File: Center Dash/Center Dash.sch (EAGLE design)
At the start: 55 parts, among them J1 502585-0470, U2 TPS54540DDARQ1

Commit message: Fixed Ashers fuck up
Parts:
- added R3, R5, R9: 100, rcl:R-US_R0805
- C1, C11, C13, C14, C15, C16, C2, C3, C4, C5, C6, C7: value (none) -> 10uF; device rcl:C-USC0402 -> rcl:C-USC0603K; PARTNO (none) -> GRM188R61A106KE69D
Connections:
- removed net SPARE_4: U$1.P7, U$2.36/A17
- removed net SPARE_5: U$1.P6, U$2.37/A18
- new net IGNITION_1: R5.2, U$1.P12, U$2.33/A14
- new net IGNITION_2: R3.2, U$1.P11, U$2.34/A15
- new net N$11: LED1.DI, R9.1
- net +3V3: now also R3.1, R5.1
- net DI1: now also R9.2; no longer LED1.DI
- net SPARE_1: now also U$1.P8, U$2.35/A16; no longer U$1.P12, U$2.33/A14
- net SPARE_2: now also U$1.P7, U$2.36/A17; no longer U$1.P11, U$2.34/A15
- net SPARE_3: now also U$1.P6, U$2.37/A18; no longer U$1.P8, U$2.35/A16
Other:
- moved on the sheet: C1, C11, C13, C14, C15, C16, C2, C3, C4, C5, C6, C7

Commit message: Made changes
Change LED caps to .1uF on right ear and center
Add resistor to D2
Add level shifters (1 for D1, 1 for D2)
Add mount holes on right ear
Add mosfet for servo (see things to consider.txt)
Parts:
- added R11: 100, rcl:R-US_R0805
- C1, C11, C13, C14, C15, C16, C2, C3, C4, C5, C6, C7: value 10uF -> .1uF
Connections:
- new net DI2_MORE: R11.1, U$1.P4
- net DI2: now also R11.2; no longer U$1.P4
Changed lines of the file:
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@@
 <?xml version="1.0" encoding="utf-8"?>
 <!DOCTYPE eagle SYSTEM "eagle.dtd">
-<eagle version="8.5.0">
+<eagle version="8.3.1">
 <drawing>
 <settings>
@@
 <part name="+3V1" library="supply1" library_urn="urn:adsk.eagle:library:371" deviceset="+3V3" device=""/>
 <part name="R9" library="rcl" deviceset="R-US_" device="R0805" value="100"/>
-<part name="C1" library="rcl" deviceset="C-US" device="C0603K" value="10uF">
+<part name="C1" library="rcl" deviceset="C-US" device="C0603K" value=".1uF">
 <attribute name="PARTNO" value="GRM188R61A106KE69D"/>
 </part>
-<part name="C2" library="rcl" deviceset="C-US" device="C0603K" value="10uF">
+<part name="C2" library="rcl" deviceset="C-US" device="C0603K" value=".1uF">
 <attribute name="PARTNO" value="GRM188R61A106KE69D"/>
 </part>
-<part name="C3" library="rcl" deviceset="C-US" device="C0603K" value="10uF">
+<part name="C3" library="rcl" deviceset="C-US" device="C0603K" value=".1uF">
 <attribute name="PARTNO" value="GRM188R61A106KE69D"/>
 </part>
-<part name="C4" library="rcl" deviceset="C-US" device="C0603K" value="10uF">
+<part name="C4" library="rcl" deviceset="C-US" device="C0603K" value=".1uF">
 <attribute name="PARTNO" value="GRM188R61A106KE69D"/>
 </part>
-<part name="C5" library="rcl" deviceset="C-US" device="C0603K" value="10uF">
+<part name="C5" library="rcl" deviceset="C-US" device="C0603K" value=".1uF">
 <attribute name="PARTNO" value="GRM188R61A106KE69D"/>
 </part>
-<part name="C6" library="rcl" deviceset="C-US" device="C0603K" value="10uF">
+<part name="C6" library="rcl" deviceset="C-US" device="C0603K" value=".1uF">
 <attribute name="PARTNO" value="GRM188R61A106KE69D"/>
 </part>
-<part name="C7" library="rcl" deviceset="C-US" device="C0603K" value="10uF">
+<part name="C7" library="rcl" deviceset="C-US" device="C0603K" value=".1uF">
 <attribute name="PARTNO" value="GRM188R61A106KE69D"/>
 </part>
-<part name="C11" library="rcl" deviceset="C-US" device="C0603K" value="10uF">
+<part name="C11" library="rcl" deviceset="C-US" device="C0603K" value=".1uF">
 <attribute name="PARTNO" value="GRM188R61A106KE69D"/>
 </part>
-<part name="C13" library="rcl" deviceset="C-US" device="C0603K" value="10uF">
+<part name="C13" library="rcl" deviceset="C-US" device="C0603K" value=".1uF">
 <attribute name="PARTNO" value="GRM188R61A106KE69D"/>
 </part>
-<part name="C14" library="rcl" deviceset="C-US" device="C0603K" value="10uF">
+<part name="C14" library="rcl" deviceset="C-US" device="C0603K" value=".1uF">
 <attribute name="PARTNO" value="GRM188R61A106KE69D"/>
 </part>
-<part name="C15" library="rcl" deviceset="C-US" device="C0603K" value="10uF">
+<part name="C15" library="rcl" deviceset="C-US" device="C0603K" value=".1uF">
 <attribute name="PARTNO" value="GRM188R61A106KE69D"/>
 </part>
-<part name="C16" library="rcl" deviceset="C-US" device="C0603K" value="10uF">
+<part name="C16" library="rcl" deviceset="C-US" device="C0603K" value=".1uF">
 <attribute name="PARTNO" value="GRM188R61A106KE69D"/>
 </part>
+<part name="R11" library="rcl" deviceset="R-US_" device="R0805" value="100"/>
 </parts>
 <sheets>
@@
 <attribute name="PARTNO" x="203.2" y="-114.3" size="1.778" layer="96" display="off"/>
 </instance>
+<instance part="R11" gate="G$1" x="322.58" y="-236.22" rot="R180"/>
 </instances>
 <busses>
@@
 <net name="DI2" class="0">
 <segment>
-<pinref part="U$1" gate="G$1" pin="P4"/>
-<wire x1="391.16" y1="-226.06" x2="401.32" y2="-226.06" width="0.1524" layer="91"/>
-<label x="396.24" y="-226.06" size="1.778" layer="95"/>
-</segment>
-<segment>
 <pinref part="U$2" gate="G$1" pin="21/A7"/>
-<wire x1="274.32" y1="-236.22" x2="304.8" y2="-236.22" width="0.1524" layer="91"/>
+<wire x1="274.32" y1="-236.22" x2="317.5" y2="-236.22" width="0.1524" layer="91"/>
 <label x="299.72" y="-236.22" size="1.778" layer="95"/>
+<pinref part="R11" gate="G$1" pin="2"/>
 </segment>
 </net>
@@
 </segment>
 </net>
+<net name="DI2_MORE" class="0">
+<segment>
+<pinref part="R11" gate="G$1" pin="1"/>
+<wire x1="327.66" y1="-236.22" x2="340.36" y2="-236.22" width="0.1524" layer="91"/>
+<label x="330.2" y="-236.22" size="1.778" layer="95"/>
+</segment>
+<segment>
+<pinref part="U$1" gate="G$1" pin="P4"/>
+<wire x1="391.16" y1="-226.06" x2="401.32" y2="-226.06" width="0.1524" layer="91"/>
+<label x="396.24" y="-226.06" size="1.778" layer="95"/>
+</segment>
+</net>

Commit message: Added level shifter to center dash
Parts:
- added U1: ADG3304BRUZ-REEL7, FormE:ADG3304
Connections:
- removed net DI1: R9.2, U$2.2
- new net DI: U$2.2, U1.A1
- new net DI_MORE: R11.1, U1.A2
- new net N$21: R9.2, U1.Y1
- net +3V3: now also U1.VCCA
- net +5V: now also U1.VCCY
- net DI2_MORE: now also U1.Y2; no longer R11.1
- net GND: now also U1.GND
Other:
- moved on the sheet: C1, C10, C11, C12, C13, C14, C15, C16, C18, C2, C24, C25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

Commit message: Done with board layouts
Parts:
- added JP3, JP4, JP7: (no value), pinhead:PINHD-1X1
- added JP5, JP6, JP8: (no value), pinhead:PINHD-1X2
- added LED13, LED14, LED15: GREEN, FormE:LEDCHIP-LED0805
- added R12: 0/DNP, rcl:R-US_R0805
- added R13, R14, R15: 1K, adafruit:R-US_R0805
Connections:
- removed net DI2: R11.2, U$2.21/A7
- new net DI2_OUT: R11.1, U$1.P4
- new net N$20: LED14.C, R14.2
- new net N$22: LED15.C, R15.2
- new net N$56: LED13.C, R13.2
- net +15V: now also LED15.A
- net +3V3: now also LED13.A
- net +5V: now also LED14.A
- net CAN_RX: now also JP6.1
- net CAN_TX: now also JP6.2
- net DI2_MORE: now also JP5.2, R11.2; no longer U$1.P4
- net DI_MORE: now also U$2.21/A7; no longer R11.1
- net GND: now also JP3.1, JP4.1, R13.1, R14.1, R15.1
- net MISO: now also JP8.1
- net MOSI: now also JP8.2
- net N$11: now also R12.1
- net N$2: now also R12.2
- net N$21: now also JP5.1
- net SERVO_PWM: now also JP7.1
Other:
- note added: "SM Power Supply"
- note removed: "Constant Current Power Supply"
- moved on the sheet: C1, C11, C13, C14, C15, C16, C2, C3, C4, C5, C6, C7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

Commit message: Worked on code
Updated board layouts since shit changed
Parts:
- added Q1, Q2, Q3, Q4: BSS138, FormE:BSS138
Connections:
- new net AMS_OUT: Q1.D, U$1.P20
- new net BSPD_OUT: Q3.D, U$1.P22
- new net IMD_OUT: Q2.D, U$1.P21
- new net TPS_OUT: Q4.D, U$1.P23
- net AMS: now also Q1.G; no longer U$1.P20
- net BSPD: now also Q3.G; no longer U$1.P22
- net GND: now also Q1.S, Q2.S, Q3.S, Q4.S
- net IMD: now also Q2.G; no longer U$1.P21
- net TPS: now also Q4.G; no longer U$1.P23
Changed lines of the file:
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@@
 <part name="JP5" library="pinhead" library_urn="urn:adsk.eagle:library:325" deviceset="PINHD-1X2" device="" package3d_urn="urn:adsk.eagle:package:22435/2"/>
 <part name="JP8" library="pinhead" library_urn="urn:adsk.eagle:library:325" deviceset="PINHD-1X2" device="" package3d_urn="urn:adsk.eagle:package:22435/2"/>
+<part name="Q1" library="FormE" deviceset="BSS138" device=""/>
+<part name="Q2" library="FormE" deviceset="BSS138" device=""/>
+<part name="Q3" library="FormE" deviceset="BSS138" device=""/>
+<part name="Q4" library="FormE" deviceset="BSS138" device=""/>
+<part name="GND33" library="supply1" deviceset="GND" device=""/>
 </parts>
 <sheets>
@@
 <instance part="GND1" gate="1" x="177.8" y="-431.8"/>
 <instance part="P+2" gate="1" x="177.8" y="-408.94"/>
-<instance part="GND2" gate="1" x="177.8" y="-241.3"/>
+<instance part="GND2" gate="1" x="177.8" y="-228.6"/>
 <instance part="GND3" gate="1" x="302.26" y="-147.32"/>
 <instance part="GND5" gate="1" x="304.8" y="-104.14"/>
@@
 <instance part="JP5" gate="G$1" x="259.08" y="-154.94"/>
 <instance part="JP8" gate="G$1" x="177.8" y="-294.64" rot="R180"/>
+<instance part="Q1" gate="G$1" x="53.34" y="-246.38" rot="MR0"/>
+<instance part="Q2" gate="G$1" x="40.64" y="-256.54" rot="MR0"/>
+<instance part="Q3" gate="G$1" x="30.48" y="-266.7" rot="MR0"/>
+<instance part="Q4" gate="G$1" x="22.86" y="-279.4" rot="MR0"/>
+<instance part="GND33" gate="1" x="22.86" y="-289.56"/>
 </instances>
 <busses>
@@
 <pinref part="GND2" gate="1" pin="GND"/>
 <wire x1="182.88" y1="-223.52" x2="177.8" y2="-223.52" width="0.1524" layer="91"/>
-<wire x1="177.8" y1="-223.52" x2="177.8" y2="-238.76" width="0.1524" layer="91"/>
+<wire x1="177.8" y1="-223.52" x2="177.8" y2="-226.06" width="0.1524" layer="91"/>
 <pinref part="JP3" gate="G$1" pin="1"/>
 <wire x1="182.88" y1="-215.9" x2="182.88" y2="-223.52" width="0.1524" layer="91"/>
@@
 <wire x1="-27.94" y1="-109.22" x2="-27.94" y2="-106.68" width="0.1524" layer="91"/>
 <pinref part="R15" gate="G$1" pin="1"/>
+</segment>
+<segment>
+<pinref part="GND33" gate="1" pin="GND"/>
+<pinref part="Q4" gate="G$1" pin="S"/>
+<wire x1="22.86" y1="-287.02" x2="22.86" y2="-281.94" width="0.1524" layer="91"/>
+<pinref part="Q3" gate="G$1" pin="S"/>
+<wire x1="30.48" y1="-269.24" x2="30.48" y2="-287.02" width="0.1524" layer="91"/>
+<wire x1="30.48" y1="-287.02" x2="22.86" y2="-287.02" width="0.1524" layer="91"/>
+<junction x="22.86" y="-287.02"/>
+<pinref part="Q2" gate="G$1" pin="S"/>
+<wire x1="40.64" y1="-259.08" x2="40.64" y2="-287.02" width="0.1524" layer="91"/>
+<wire x1="40.64" y1="-287.02" x2="30.48" y2="-287.02" width="0.1524" layer="91"/>
+<junction x="30.48" y="-287.02"/>
+<pinref part="Q1" gate="G$1" pin="S"/>
+<wire x1="53.34" y1="-248.92" x2="53.34" y2="-287.02" width="0.1524" layer="91"/>
+<wire x1="53.34" y1="-287.02" x2="40.64" y2="-287.02" width="0.1524" layer="91"/>
+<junction x="40.64" y="-287.02"/>
 </segment>
 </net>
@@
 <segment>
 <pinref part="U$2" gate="G$1" pin="5"/>
-<wire x1="233.68" y1="-238.76" x2="220.98" y2="-238.76" width="0.1524" layer="91"/>
 <label x="220.98" y="-238.76" size="1.778" layer="95"/>
-</segment>
-<segment>
-<pinref part="U$1" gate="G$1" pin="P20"/>
-<wire x1="391.16" y1="-271.78" x2="454.66" y2="-271.78" width="0.1524" layer="91"/>
-<label x="449.58" y="-271.78" size="1.778" layer="95"/>
+<wire x1="233.68" y1="-238.76" x2="68.58" y2="-238.76" width="0.1524" layer="91"/>
+<pinref part="Q1" gate="G$1" pin="G"/>
+<wire x1="68.58" y1="-238.76" x2="68.58" y2="-246.38" width="0.1524" layer="91"/>
+<wire x1="68.58" y1="-246.38" x2="58.42" y2="-246.38" width="0.1524" layer="91"/>
 </segment>
 </net>
@@
 <segment>
 <pinref part="U$2" gate="G$1" pin="6"/>
-<wire x1="233.68" y1="-241.3" x2="220.98" y2="-241.3" width="0.1524" layer="91"/>
 <label x="220.98" y="-241.3" size="1.778" layer="95"/>
-</segment>
-<segment>
-<pinref part="U$1" gate="G$1" pin="P21"/>
-<wire x1="391.16" y1="-274.32" x2="454.66" y2="-274.32" width="0.1524" layer="91"/>
-<label x="449.58" y="-274.32" size="1.778" layer="95"/>
+<wire x1="233.68" y1="-241.3" x2="73.66" y2="-241.3" width="0.1524" layer="91"/>
+<wire x1="73.66" y1="-241.3" x2="73.66" y2="-256.54" width="0.1524" layer="91"/>
+<pinref part="Q2" gate="G$1" pin="G"/>
+<wire x1="73.66" y1="-256.54" x2="45.72" y2="-256.54" width="0.1524" layer="91"/>
 </segment>
 </net>
@@
 <segment>
 <pinref part="U$2" gate="G$1" pin="7"/>
-<wire x1="233.68" y1="-243.84" x2="220.98" y2="-243.84" width="0.1524" layer="91"/>
 <label x="220.98" y="-243.84" size="1.778" layer="95"/>
-</segment>
-<segment>
-<pinref part="U$1" gate="G$1" pin="P22"/>
-<wire x1="391.16" y1="-276.86" x2="454.66" y2="-276.86" width="0.1524" layer="91"/>
-<label x="449.58" y="-276.86" size="1.778" layer="95"/>
+<wire x1="233.68" y1="-243.84" x2="76.2" y2="-243.84" width="0.1524" layer="91"/>
+<wire x1="76.2" y1="-243.84" x2="76.2" y2="-266.7" width="0.1524" layer="91"/>
+<pinref part="Q3" gate="G$1" pin="G"/>
+<wire x1="76.2" y1="-266.7" x2="35.56" y2="-266.7" width="0.1524" layer="91"/>
 </segment>
 </net>
@@
 <segment>
 <pinref part="U$2" gate="G$1" pin="8"/>
-<wire x1="233.68" y1="-246.38" x2="220.98" y2="-246.38" width="0.1524" layer="91"/>
 <label x="220.98" y="-246.38" size="1.778" layer="95"/>
-</segment>
-<segment>
-<pinref part="U$1" gate="G$1" pin="P23"/>
-<wire x1="391.16" y1="-279.4" x2="454.66" y2="-279.4" width="0.1524" layer="91"/>
-<label x="449.58" y="-279.4" size="1.778" layer="95"/>
+<wire x1="233.68" y1="-246.38" x2="78.74" y2="-246.38" width="0.1524" layer="91"/>
+<wire x1="78.74" y1="-246.38" x2="78.74" y2="-279.4" width="0.1524" layer="91"/>
+<pinref part="Q4" gate="G$1" pin="G"/>
+<wire x1="78.74" y1="-279.4" x2="27.94" y2="-279.4" width="0.1524" layer="91"/>
 </segment>
 </net>
@@
 </segment>
 </net>
+<net name="AMS_OUT" class="0">
+<segment>
+<pinref part="Q1" gate="G$1" pin="D"/>
+<wire x1="53.34" y1="-238.76" x2="17.78" y2="-238.76" width="0.1524" layer="91"/>
+<label x="17.78" y="-238.76" size="1.778" layer="95"/>
+</segment>
+<segment>
+<pinref part="U$1" gate="G$1" pin="P20"/>
+<wire x1="391.16" y1="-271.78" x2="454.66" y2="-271.78" width="0.1524" layer="91"/>
+<label x="444.5" y="-271.78" size="1.778" layer="95"/>
+</segment>
+</net>
+<net name="IMD_OUT" class="0">
+<segment>
+<pinref part="Q2" gate="G$1" pin="D"/>
+<wire x1="40.64" y1="-248.92" x2="40.64" y2="-241.3" width="0.1524" layer="91"/>
+<wire x1="40.64" y1="-241.3" x2="17.78" y2="-241.3" width="0.1524" layer="91"/>
+<label x="17.78" y="-241.3" size="1.778" layer="95"/>
+</segment>
+<segment>
+<pinref part="U$1" gate="G$1" pin="P21"/>
+<wire x1="391.16" y1="-274.32" x2="454.66" y2="-274.32" width="0.1524" layer="91"/>
+<label x="444.5" y="-274.32" size="1.778" layer="95"/>
+</segment>
+</net>
+<net name="BSPD_OUT" class="0">
+<segment>
+<pinref part="Q3" gate="G$1" pin="D"/>
+<wire x1="30.48" y1="-259.08" x2="30.48" y2="-243.84" width="0.1524" layer="91"/>
+<wire x1="30.48" y1="-243.84" x2="17.78" y2="-243.84" width="0.1524" layer="91"/>
+<label x="17.78" y="-243.84" size="1.778" layer="95"/>
+</segment>
+<segment>
+<pinref part="U$1" gate="G$1" pin="P22"/>
+<wire x1="391.16" y1="-276.86" x2="454.66" y2="-276.86" width="0.1524" layer="91"/>
+<label x="444.5" y="-276.86" size="1.778" layer="95"/>
+</segment>
+</net>
+<net name="TPS_OUT" class="0">
+<segment>
+<pinref part="Q4" gate="G$1" pin="D"/>
+<wire x1="22.86" y1="-271.78" x2="22.86" y2="-246.38" width="0.1524" layer="91"/>
+<wire x1="22.86" y1="-246.38" x2="17.78" y2="-246.38" width="0.1524" layer="91"/>
+<label x="17.78" y="-246.38" size="1.778" layer="95"/>
+</segment>
+<segment>
+<pinref part="U$1" gate="G$1" pin="P23"/>
+<wire x1="391.16" y1="-279.4" x2="454.66" y2="-279.4" width="0.1524" layer="91"/>
+<label x="444.5" y="-279.4" size="1.778" layer="95"/>
+</segment>
+</net>

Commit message: Fix for daqbus CAN
Added another can transceiver for the daq bus
Moved the ignition1 and 2 to different pins to account for the teensy can bus lines
Fixed the can code from flexcan
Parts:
- added C17, C21: .1uF, rcl:C-USC0805
- added JP9: (no value), pinhead:PINHD-1X2
- added R16: 120, rcl:R-US_R0805
- added U4: (no value), FormE:MCP256X-SOIC
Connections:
- net CAN_N renamed CARCAN_N
- net CAN_P renamed CARCAN_P
- net CAN_RX renamed CARCAN_RX
- net CAN_TX renamed CARCAN_TX
- removed net SPARE_2: U$1.P7, U$2.36/A17
- removed net SPARE_3: U$1.P6, U$2.37/A18
- new net DAQCAN_N: R16.2, U$1.P7, U4.CANL
- new net DAQCAN_P: R16.1, U$1.P6, U4.CANH
- new net DAQCAN_RX: JP9.2, U$2.34/A15, U4.RXD
- new net DAQCAN_TX: JP9.1, U$2.33/A14, U4.TXD
- net +3V3: now also C21.1, U4.SPLIT/VIO
- net +5V: now also C17.1, U4.VDD
- net GND: now also C17.2, C21.2, U4.STBY, U4.VSS
- net IGNITION_1: now also R3.2, U$1.P11, U$2.35/A16; no longer R5.2, U$1.P12, U$2.33/A14
- net IGNITION_2: now also R5.2, U$1.P12, U$2.36/A17; no longer R3.2, U$1.P11, U$2.34/A15
- net SPARE_1: now also U$2.37/A18; no longer U$2.35/A16
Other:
- note added: "CARCAN Transiever"
- note added: "DAQCAN Transiever"
- note removed: "CAN Transiever"

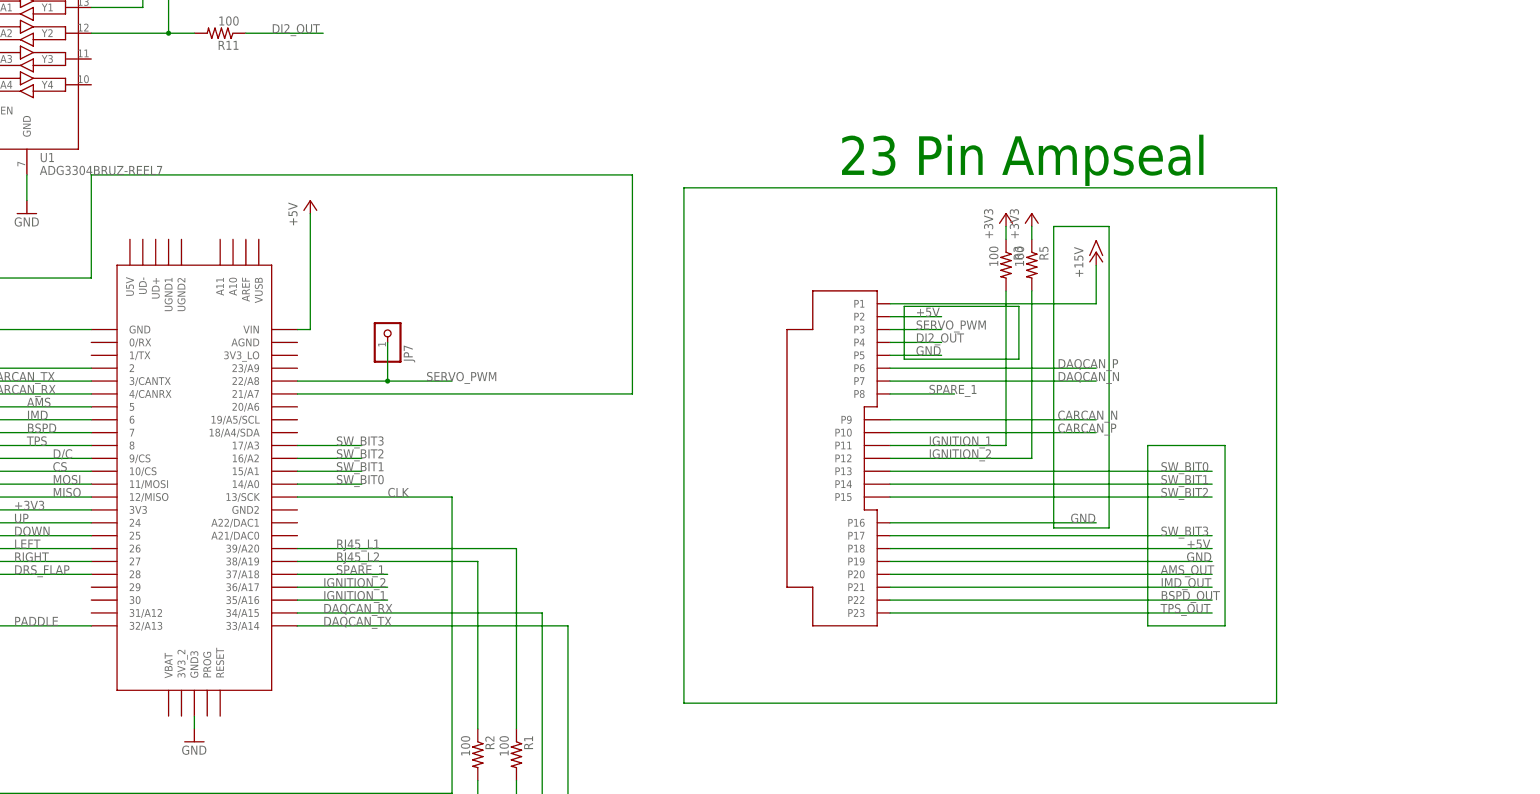
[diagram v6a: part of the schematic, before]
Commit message: Add voltage dividers to 5V input lines
Now we can use Teensy 3.6
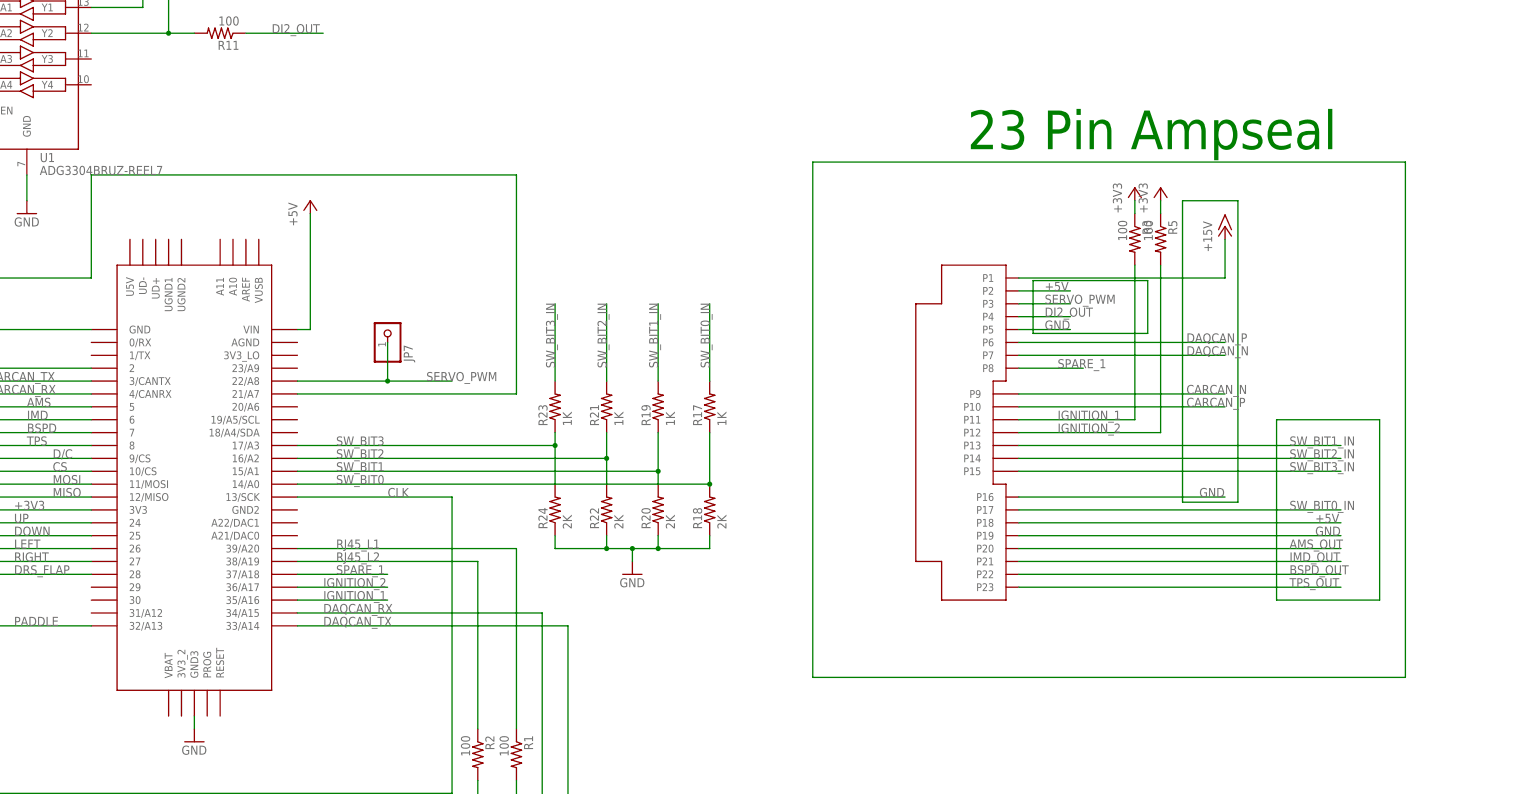
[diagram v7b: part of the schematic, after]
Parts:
- added R17, R19, R21, R23: 1K, adafruit:R-US_R0805
- added R18, R20, R22, R24: 2K, adafruit:R-US_R0805
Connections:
- new net SW_BIT0_IN: R17.2, U$1.P17
- new net SW_BIT1_IN: R19.2, U$1.P13
- new net SW_BIT2_IN: R21.2, U$1.P14
- new net SW_BIT3_IN: R23.2, U$1.P15
- net GND: now also R18.1, R20.1, R22.1, R24.1
- net SW_BIT0: now also R17.1, R18.2; no longer U$1.P13
- net SW_BIT1: now also R19.1, R20.2; no longer U$1.P14
- net SW_BIT2: now also R21.1, R22.2; no longer U$1.P15
- net SW_BIT3: now also R23.1, R24.2; no longer U$1.P17
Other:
- moved on the sheet: R3, R5
